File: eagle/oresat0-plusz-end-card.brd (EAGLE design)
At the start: 99.8 x 94.6 mm, 36 parts, among them J1 Harwin M55-7101242R, J2 Harwin M55-7101242R, J3 Harwin M55-7101242R, J4 Harwin M55-7101242R, J6 J-SAMTEC-TFM-120-X1-XXX-D-RA, U1 QCN-19D+, U2 QCN-19D+, U3 QCN-19D+

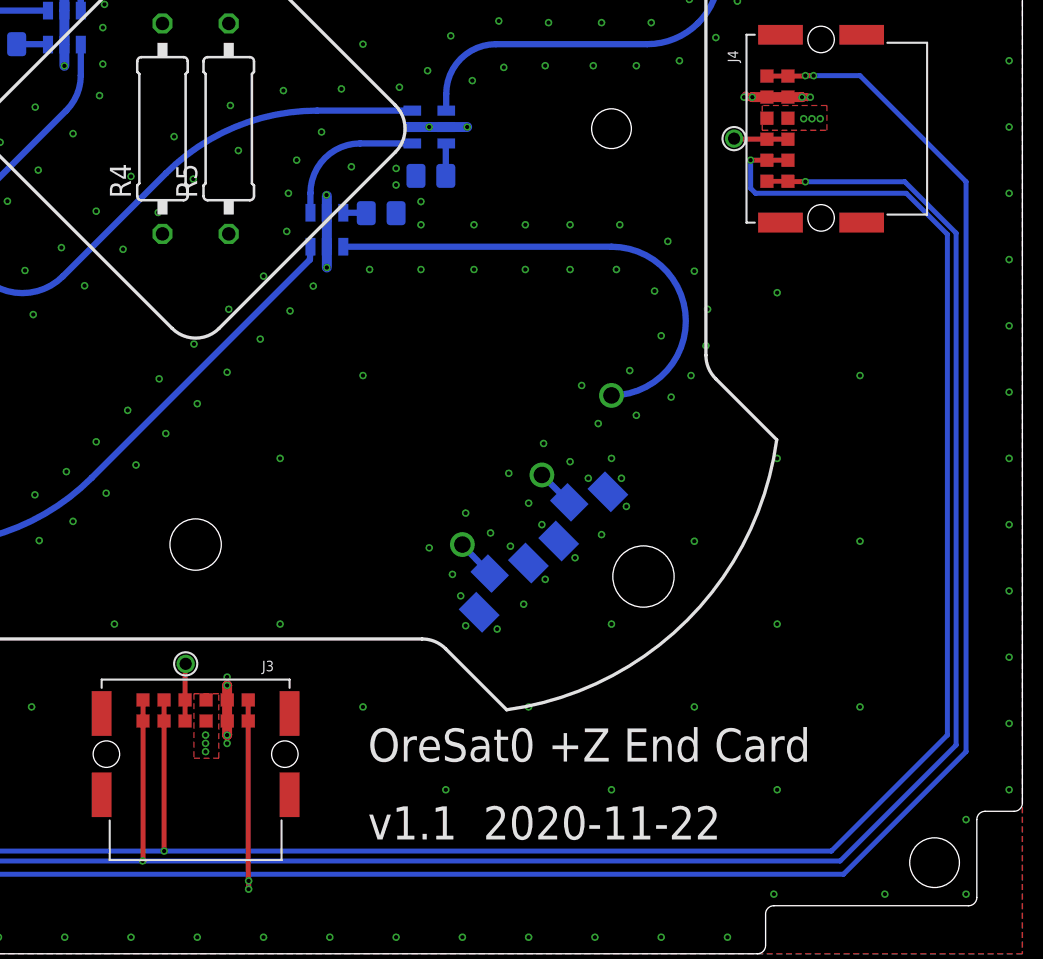
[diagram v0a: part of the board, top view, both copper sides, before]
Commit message: Final cleanup and polish of v1.1 OreSat0 +Z end card and mezzanine. Fixed S band 1/4 wave, lots of stiching and polish, fixed radial TCREAM on the contact pads, lots of TNAMES polish.
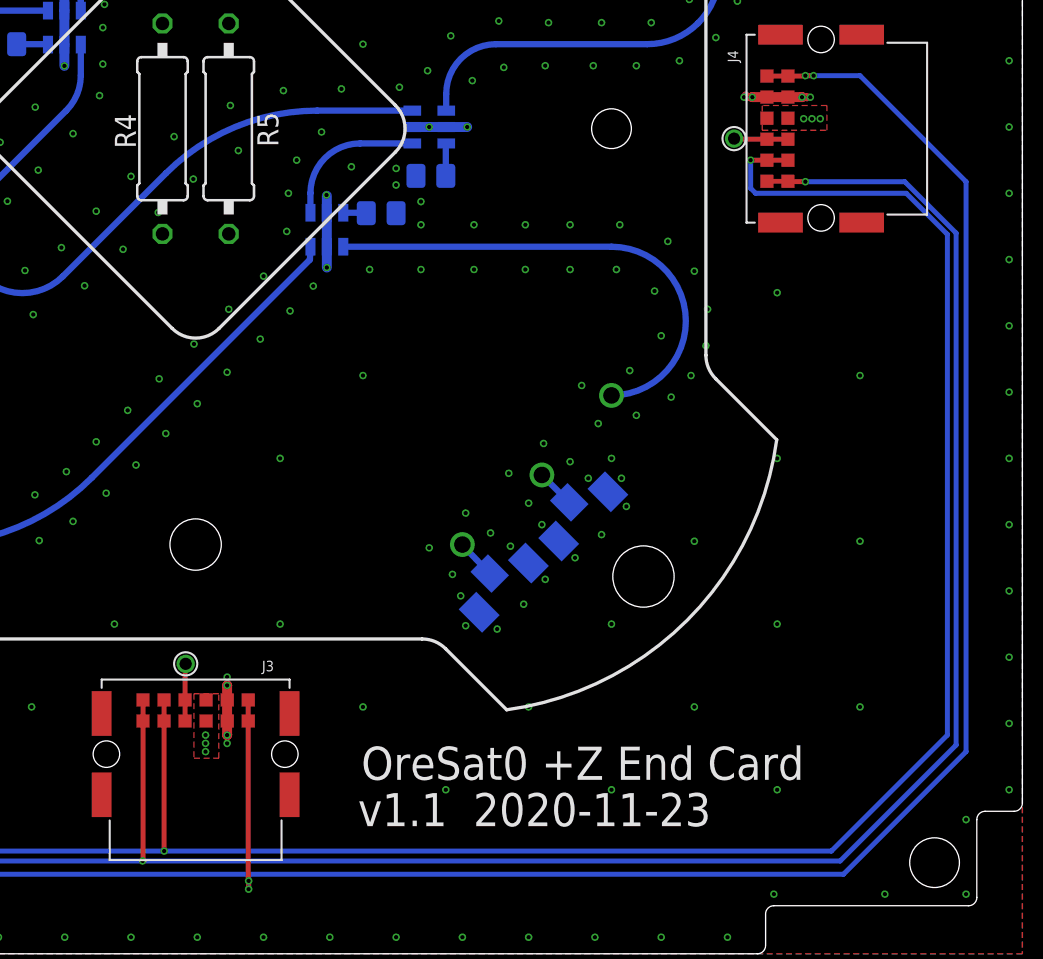
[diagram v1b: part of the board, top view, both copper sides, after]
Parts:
- R4: value HOT -> 1 1W
- R5: value WARMISH -> 1 1W
- renumbered U$1 to J12, U$13 to J15, U$14 to J16, U$2 to J13, U$3 to J14, U$4 to J7, U$5 to J8, U$6 to J9, U$7 to J10, U$8 to J11
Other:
- board text added: "v1.1 2020-11-23"
- board text removed: "v1.1 2020-11-22"

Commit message: Clean up BOM and part numbers. Ready for v1.1 fab.
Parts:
- renumbered U$10 to HW2, U$11 to HW3, U$12 to HW4, U$9 to HW1
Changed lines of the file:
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@@
 <attribute name="P-NP" value="P" x="77.9" y="90.6" locked="yes" size="1.778" layer="27" display="off"/>
 </element>
-<element name="U$9" library="HW-mcmaster-94100A150-M2-threaded-insert" package="MCMASTER-94100A150" value="MCMASTER-94100A150" x="76.93" y="76.83" smashed="yes"/>
-<element name="U$10" library="HW-mcmaster-94100A150-M2-threaded-insert" package="MCMASTER-94100A150" value="MCMASTER-94100A150" x="76.93" y="22.77" smashed="yes"/>
-<element name="U$11" library="HW-mcmaster-94100A150-M2-threaded-insert" package="MCMASTER-94100A150" value="MCMASTER-94100A150" x="22.87" y="76.83" smashed="yes"/>
-<element name="U$12" library="HW-mcmaster-94100A150-M2-threaded-insert" package="MCMASTER-94100A150" value="MCMASTER-94100A150" x="22.87" y="22.77" smashed="yes"/>
+<element name="HW1" library="HW-mcmaster-94100A150-M2-threaded-insert" package="MCMASTER-94100A150" value="MCMASTER-94100A150" x="76.93" y="76.83" smashed="yes"/>
+<element name="HW2" library="HW-mcmaster-94100A150-M2-threaded-insert" package="MCMASTER-94100A150" value="MCMASTER-94100A150" x="76.93" y="22.77" smashed="yes"/>
+<element name="HW3" library="HW-mcmaster-94100A150-M2-threaded-insert" package="MCMASTER-94100A150" value="MCMASTER-94100A150" x="22.87" y="76.83" smashed="yes"/>
+<element name="HW4" library="HW-mcmaster-94100A150-M2-threaded-insert" package="MCMASTER-94100A150" value="MCMASTER-94100A150" x="22.87" y="22.77" smashed="yes"/>
 <element name="PCB1" library="oresat-cards" package="ORESAT-CARD-V1.3-GENERIC-3RF" value="ORESAT-CARD-V1.3-GENERIC-3RF" x="0" y="0" locked="yes" smashed="yes"/>
 <element name="CM1" library="J-Molex-73300-003X-SMPM-M-edge-mount-NO-DIM" package="J-MOLEX-SMPM-073300-003X" value="J-MOLEX-SMPM-73300-003X" x="71.9" y="90.6" locked="yes" smashed="yes">

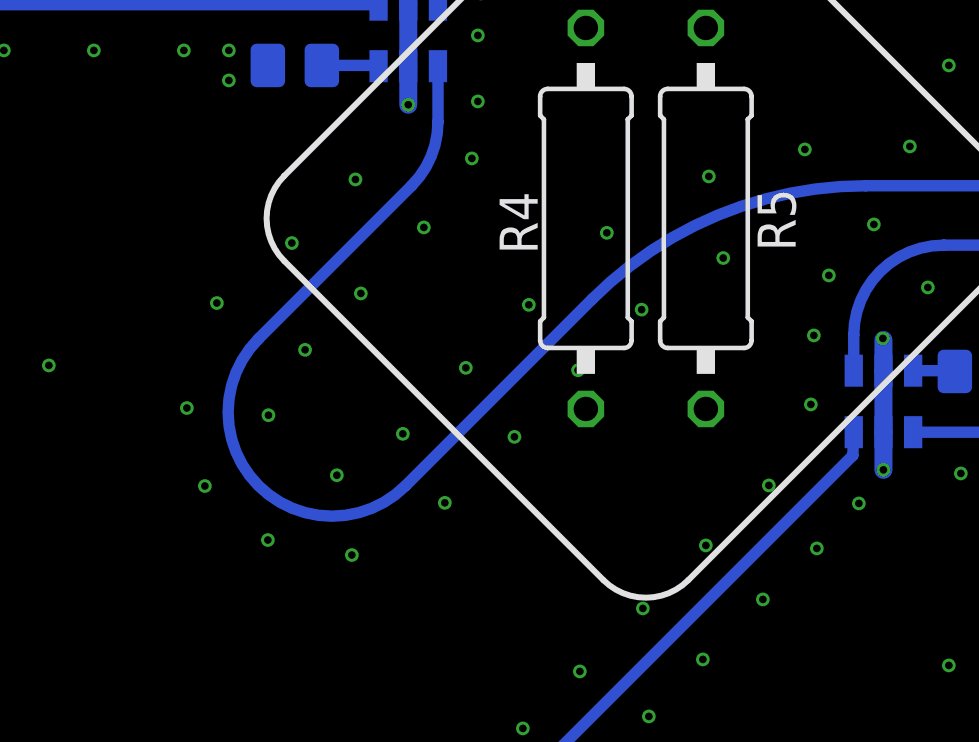
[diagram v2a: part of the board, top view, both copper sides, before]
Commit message: Switched to a QCN-27D+ (with DC passthrough) for S band, and made the U and L band 1/4 wave lengths a bit more precise after getting precise lengths from Eric.
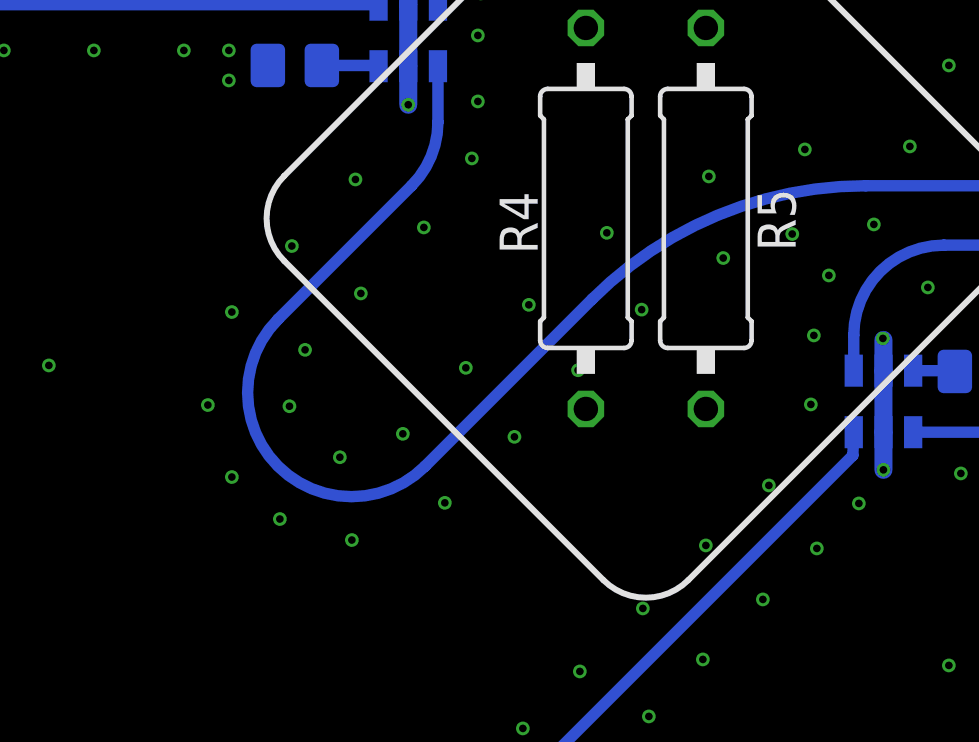
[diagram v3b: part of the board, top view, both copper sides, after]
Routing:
- net LBAND-1/4L: track 42.7 -> 40.9 mm
- net GND: vias 426 -> 427
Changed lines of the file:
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@@
 <layer number="14" name="Route14" color="22" fill="1" visible="no" active="no"/>
 <layer number="15" name="Route15" color="23" fill="1" visible="no" active="yes"/>
-<layer number="16" name="Bottom" color="1" fill="1" visible="yes" active="yes"/>
+<layer number="16" name="Bottom" color="1" fill="1" visible="no" active="yes"/>
 <layer number="17" name="Pads" color="2" fill="1" visible="yes" active="yes"/>
 <layer number="18" name="Vias" color="2" fill="1" visible="yes" active="yes"/>
@@
 <layer number="20" name="Dimension" color="24" fill="1" visible="yes" active="yes"/>
 <layer number="21" name="tPlace" color="7" fill="1" visible="yes" active="yes"/>
-<layer number="22" name="bPlace" color="7" fill="1" visible="yes" active="yes"/>
+<layer number="22" name="bPlace" color="7" fill="1" visible="no" active="yes"/>
 <layer number="23" name="tOrigins" color="15" fill="1" visible="yes" active="yes"/>
-<layer number="24" name="bOrigins" color="15" fill="1" visible="yes" active="yes"/>
+<layer number="24" name="bOrigins" color="15" fill="1" visible="no" active="yes"/>
 <layer number="25" name="tNames" color="7" fill="1" visible="yes" active="yes"/>
-<layer number="26" name="bNames" color="7" fill="1" visible="yes" active="yes"/>
+<layer number="26" name="bNames" color="7" fill="1" visible="no" active="yes"/>
 <layer number="27" name="tValues" color="7" fill="1" visible="no" active="yes"/>
 <layer number="28" name="bValues" color="7" fill="1" visible="no" active="yes"/>
 <layer number="29" name="tStop" color="7" fill="3" visible="yes" active="yes"/>
-<layer number="30" name="bStop" color="7" fill="6" visible="yes" active="yes"/>
+<layer number="30" name="bStop" color="7" fill="6" visible="no" active="yes"/>
 <layer number="31" name="tCream" color="7" fill="4" visible="no" active="yes"/>
 <layer number="32" name="bCream" color="7" fill="5" visible="no" active="yes"/>
@@
 <wire x1="61.405" y1="50.89" x2="56.232640625" y2="50.89" width="1.5" layer="30"/>
 <wire x1="56.232640625" y1="50.89" x2="46.611321875" y2="45.511321875" width="1.5" layer="30" curve="45"/>
-<wire x1="46.611321875" y1="45.511321875" x2="41.29" y2="40.29" width="1.5" layer="30"/>
-<wire x1="41.29" y1="40.29" x2="37.74" y2="46.44" width="1.5" layer="30" curve="-180"/>
-<wire x1="37.74" y1="46.44" x2="42.091321875" y2="50.891321875" width="1.5" layer="30"/>
+<wire x1="46.611321875" y1="45.511321875" x2="41.99" y2="40.99" width="1.5" layer="30"/>
+<wire x1="41.99" y1="40.99" x2="38.44" y2="47.14" width="1.5" layer="30" curve="-180"/>
+<wire x1="38.44" y1="47.14" x2="42.091321875" y2="50.891321875" width="1.5" layer="30"/>
 <wire x1="42.091321875" y1="50.891321875" x2="42.97" y2="53.312640625" width="1.5" layer="30" curve="45"/>
 <wire x1="39.79" y1="56.925" x2="24.8" y2="56.925" width="1.18" layer="30"/>
@@
 <via x="45.52" y="42.52" extent="1-16" drill="0.254"/>
 <via x="43.2" y="40.32" extent="1-16" drill="0.254"/>
-<via x="39.6" y="41.24" extent="1-16" drill="0.254"/>
-<via x="37.32" y="43.24" extent="1-16" drill="0.254"/>
+<via x="39.7" y="41.84" extent="1-16" drill="0.254"/>
+<via x="38.02" y="43.54" extent="1-16" drill="0.254"/>
 <via x="40.4" y="47.3" extent="1-16" drill="0.254"/>
 <via x="42.5" y="49.5" extent="1-16" drill="0.254"/>
 <via x="44.1" y="51.8" extent="1-16" drill="0.254"/>
-<via x="40.1" y="38.58" extent="1-16" drill="0.254"/>
-<via x="37.3" y="39.08" extent="1-16" drill="0.254"/>
-<via x="34.6" y="43.48" extent="1-16" drill="0.254"/>
-<via x="35.6" y="46.98" extent="1-16" drill="0.254"/>
-<via x="38.1" y="48.98" extent="1-16" drill="0.254"/>
+<via x="40.1" y="39.08" extent="1-16" drill="0.254"/>
+<via x="37.7" y="39.78" extent="1-16" drill="0.254"/>
+<via x="35.3" y="43.58" extent="1-16" drill="0.254"/>
+<via x="36.1" y="46.68" extent="1-16" drill="0.254"/>
+<via x="38.1" y="48.88" extent="1-16" drill="0.254"/>
 <via x="40.22" y="51.1" extent="1-16" drill="0.254"/>
 <via x="44.3" y="53.7" extent="1-16" drill="0.254"/>
@@
 <via x="55.6" y="38.8" extent="1-16" drill="0.254"/>
 <via x="57" y="40.3" extent="1-16" drill="0.254"/>
-<via x="35.2" y="40.88" extent="1-16" drill="0.254"/>
+<via x="36.1" y="41.18" extent="1-16" drill="0.254"/>
 <via x="41.8" y="42.62" extent="1-16" drill="0.254"/>
 <via x="43.9" y="44.82" extent="1-16" drill="0.254"/>
@@
 <via x="71.4" y="79.1" extent="1-16" drill="0.254"/>
 <via x="69.2" y="78.6" extent="1-16" drill="0.254"/>
+<via x="54.78" y="49.28" extent="1-16" drill="0.254"/>
 </signal>
 <signal name="N$4">
@@
 <wire x1="62.975" y1="50.89" x2="57.232640625" y2="50.89" width="0.38" layer="16"/>
 <wire x1="57.232640625" y1="50.89" x2="48.112190625" y2="47.112190625" width="0.38" layer="16" curve="45"/>
-<wire x1="48.112190625" y1="47.112190625" x2="41.89" y2="40.89" width="0.38" layer="16"/>
-<wire x1="41.89" y1="40.89" x2="36.99" y2="45.79" width="0.38" layer="16" curve="-180"/>
-<wire x1="36.99" y1="45.79" x2="42.091321875" y2="50.891321875" width="0.38" layer="16"/>
+<wire x1="48.112190625" y1="47.112190625" x2="42.54" y2="41.54" width="0.38" layer="16"/>
+<wire x1="42.54" y1="41.54" x2="37.64" y2="46.44" width="0.38" layer="16" curve="-180"/>
+<wire x1="37.64" y1="46.44" x2="42.091321875" y2="50.891321875" width="0.38" layer="16"/>
 <wire x1="42.091321875" y1="50.891321875" x2="42.97" y2="53.012640625" width="0.38" layer="16" curve="45"/>
 <wire x1="42.97" y1="53.012640625" x2="42.97" y2="54.875" width="0.38" layer="16"/>
